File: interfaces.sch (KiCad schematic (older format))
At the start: 63 parts, among them IC3 TPD8S009DSMR, J4 WE_629105150521, J6 685119134923, J7 1140084168, Q2 BSS138AKA, Q3 BSS138AKA, Q4 BSS138AKA, Q5 BSS138AKA, Q6 BSS138AKA, U12 FT2232HQ

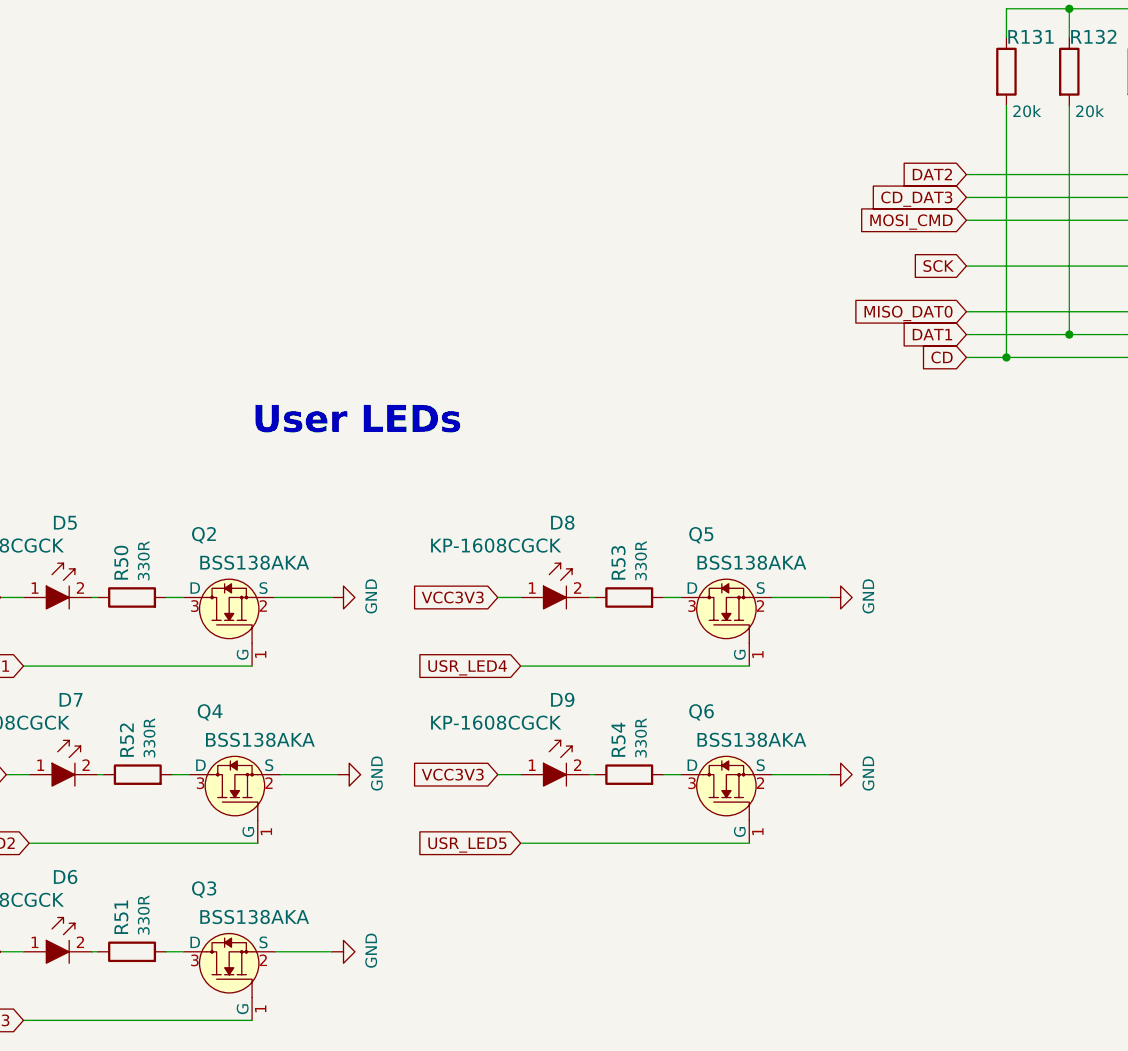
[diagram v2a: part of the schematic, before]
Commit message: Route SD card
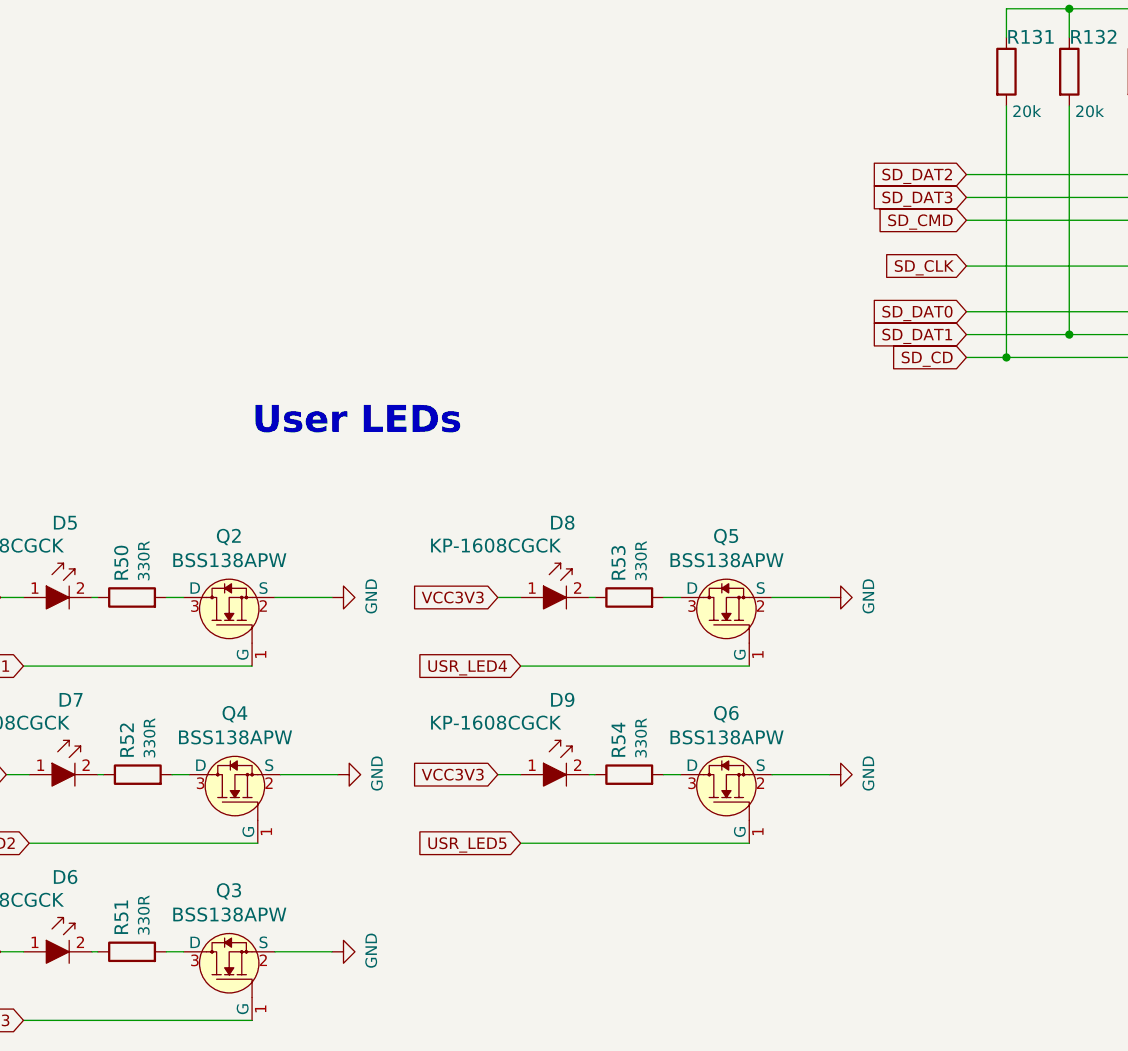
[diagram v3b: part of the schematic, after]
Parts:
- removed Q2, Q3, Q4, Q5, Q6: BSS138AKA, lpddr4-test-board-footprints:SOT-23-3, symbol lpddr4-test-board:BSS138AKA
- added Q2, Q3, Q4, Q5, Q6: BSS138APW, antmicro-footprints:SC70-3, symbol antmicroTransistorsFETsMOSFETsSingle:BSS138APW
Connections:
- net GND: now also Q2.2 (S), Q3.2 (S), Q4.2 (S), Q5.2 (S), Q6.2 (S)
- net USR_LED1: now also Q2.1 (G)
- net USR_LED2: now also Q4.1 (G)
- net USR_LED3: now also Q3.1 (G)
- net USR_LED4: now also Q5.1 (G)
- net USR_LED5: now also Q6.1 (G)
- net at R50.2: now also Q2.3 (D)
- net at R52.2: now also Q4.3 (D)
- net at R53.2: now also Q5.3 (D)
- net at R54.2: now also Q6.3 (D)
- net at R51.2: now also Q3.3 (D)
- net CD renamed SD_CD
- net CD_DAT3 renamed SD_DAT3
- net DAT1 renamed SD_DAT1
- net DAT2 renamed SD_DAT2
- net MISO_DAT0 renamed SD_DAT0
- net MOSI_CMD renamed SD_CMD
- net SCK renamed SD_CLK
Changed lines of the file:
@@
 Text GLabel 13300 6150 1    50   Input ~ 0
 VCC3V3
-Text GLabel 11125 6975 0    50   Input ~ 0
-DAT2
-Text GLabel 11125 7075 0    50   Input ~ 0
-CD_DAT3
-Text GLabel 11125 7175 0    50   Input ~ 0
-MOSI_CMD
-Text GLabel 11125 7375 0    50   Input ~ 0
-SCK
-Text GLabel 11125 7575 0    50   Input ~ 0
-MISO_DAT0
-Text GLabel 11125 7675 0    50   Input ~ 0
-DAT1
-Text GLabel 11125 7775 0    50   Input ~ 0
-CD
 Text Notes 3775 1450 0    118  ~ 24
 Debug UART
@@
 Wire Wire Line
 	7800 5900 7800 6000
-$Comp
-L lpddr4-test-board:BSS138AKA Q2
-U 1 1 5FF5BCFF
-P 7900 8825
-F 0 "Q2" V 8175 8875 60  0000 L CNN
-F 1 "BSS138AKA" V 8050 8475 60  0000 L CNN
-F 2 "lpddr4-test-board-footprints:SOT-23-3" H 8100 9025 60  0001 L CNN
-F 3 "https://www.onsemi.com/pub/Collateral/BSS138-D.PDF" H 8100 9125 60  0001 L CNN
-F 4 "BSS138AKAR" H 8100 9325 60  0001 L CNN "MPN"
-F 5 "ON Semiconductor" H 8100 9925 60  0001 L CNN "Manufacturer"
-	1    7900 8825
-	0    -1   -1   0
-$EndComp
 $Comp
 L lpddr4-test-board:GND #PWR0167
@@
 	8000 9125 7000 9125
 $Comp
-L lpddr4-test-board:BSS138AKA Q4
-U 1 1 6002240B
-P 7925 9600
-F 0 "Q4" V 8200 9650 60  0000 L CNN
-F 1 "BSS138AKA" V 8075 9250 60  0000 L CNN
-F 2 "lpddr4-test-board-footprints:SOT-23-3" H 8125 9800 60  0001 L CNN
-F 3 "https://www.onsemi.com/pub/Collateral/BSS138-D.PDF" H 8125 9900 60  0001 L CNN
-F 4 "BSS138AKAR" H 8125 10100 60  0001 L CNN "MPN"
-F 5 "ON Semiconductor" H 8125 10700 60  0001 L CNN "Manufacturer"
-	1    7925 9600
-	0    -1   -1   0
-$EndComp
-$Comp
 L lpddr4-test-board:GND #PWR0168
 U 1 1 60022411
@@
 	8025 9900 7025 9900
 $Comp
-L lpddr4-test-board:BSS138AKA Q5
-U 1 1 600304B1
-P 10075 8825
-F 0 "Q5" V 10350 8875 60  0000 L CNN
-F 1 "BSS138AKA" V 10225 8475 60  0000 L CNN
-F 2 "lpddr4-test-board-footprints:SOT-23-3" H 10275 9025 60  0001 L CNN
-F 3 "https://www.onsemi.com/pub/Collateral/BSS138-D.PDF" H 10275 9125 60  0001 L CNN
-F 4 "BSS138AKAR" H 10275 9325 60  0001 L CNN "MPN"
-F 5 "ON Semiconductor" H 10275 9925 60  0001 L CNN "Manufacturer"
-	1    10075 8825
-	0    -1   -1   0
-$EndComp
-$Comp
 L lpddr4-test-board:GND #PWR0169
 U 1 1 600304B7
@@
 	10175 9125 9175 9125
 $Comp
-L lpddr4-test-board:BSS138AKA Q6
-U 1 1 6003D8CD
-P 10075 9600
-F 0 "Q6" V 10350 9650 60  0000 L CNN
-F 1 "BSS138AKA" V 10225 9250 60  0000 L CNN
-F 2 "lpddr4-test-board-footprints:SOT-23-3" H 10275 9800 60  0001 L CNN
-F 3 "https://www.onsemi.com/pub/Collateral/BSS138-D.PDF" H 10275 9900 60  0001 L CNN
-F 4 "BSS138AKAR" H 10275 10100 60  0001 L CNN "MPN"
-F 5 "ON Semiconductor" H 10275 10700 60  0001 L CNN "Manufacturer"
-	1    10075 9600
-	0    -1   -1   0
-$EndComp
-$Comp
 L lpddr4-test-board:GND #PWR0170
 U 1 1 6003D8D3
@@
 Wire Wire Line
 	10175 9900 9175 9900
-$Comp
-L lpddr4-test-board:BSS138AKA Q3
-U 1 1 60050B08
-P 7900 10375
-F 0 "Q3" V 8175 10425 60  0000 L CNN
-F 1 "BSS138AKA" V 8050 10025 60  0000 L CNN
-F 2 "lpddr4-test-board-footprints:SOT-23-3" H 8100 10575 60  0001 L CNN
-F 3 "https://www.onsemi.com/pub/Collateral/BSS138-D.PDF" H 8100 10675 60  0001 L CNN
-F 4 "BSS138AKAR" H 8100 10875 60  0001 L CNN "MPN"
-F 5 "ON Semiconductor" H 8100 11475 60  0001 L CNN "Manufacturer"
-	1    7900 10375
-	0    -1   -1   0
-$EndComp
 $Comp
 L lpddr4-test-board:GND #PWR0171
@@
 Text Notes 8000 8125 0    118  ~ 24
 User LEDs
+$Comp
+L antmicroTransistorsFETsMOSFETsSingle:BSS138APW Q2
+U 1 1 6090FD8D
+P 7900 8825
+F 0 "Q2" V 8167 8825 60  0000 C CNN
+F 1 "BSS138APW" V 8061 8825 60  0000 C CNN
+F 2 "antmicro-footprints:SC70-3" H 8100 9025 60  0001 L CNN
+F 3 "" H 8100 9125 60  0001 L CNN
+F 4 "BSS138PW" H 8100 9325 60  0001 L CNN "MPN"
+F 5 "ON Semiconductor" H 8100 9925 60  0001 L CNN "Manufacturer"
+	1    7900 8825
+	0    -1   -1   0
+$EndComp
+$Comp
+L antmicroTransistorsFETsMOSFETsSingle:BSS138APW Q4
+U 1 1 6091F8AC
+P 7925 9600
+F 0 "Q4" V 8192 9600 60  0000 C CNN
+F 1 "BSS138APW" V 8086 9600 60  0000 C CNN
+F 2 "antmicro-footprints:SC70-3" H 8125 9800 60  0001 L CNN
+F 3 "" H 8125 9900 60  0001 L CNN
+F 4 "BSS138PW" H 8125 10100 60  0001 L CNN "MPN"
+F 5 "ON Semiconductor" H 8125 10700 60  0001 L CNN "Manufacturer"
+	1    7925 9600
+	0    -1   -1   0
+$EndComp
+$Comp
+L antmicroTransistorsFETsMOSFETsSingle:BSS138APW Q5
+U 1 1 6092108D
+P 10075 8825
+F 0 "Q5" V 10342 8825 60  0000 C CNN
+F 1 "BSS138APW" V 10236 8825 60  0000 C CNN
+F 2 "antmicro-footprints:SC70-3" H 10275 9025 60  0001 L CNN
+F 3 "" H 10275 9125 60  0001 L CNN
+F 4 "BSS138PW" H 10275 9325 60  0001 L CNN "MPN"
+F 5 "ON Semiconductor" H 10275 9925 60  0001 L CNN "Manufacturer"
+	1    10075 8825
+	0    -1   -1   0
+$EndComp
+$Comp
+L antmicroTransistorsFETsMOSFETsSingle:BSS138APW Q6
+U 1 1 60922535
+P 10075 9600
+F 0 "Q6" V 10342 9600 60  0000 C CNN
+F 1 "BSS138APW" V 10236 9600 60  0000 C CNN
+F 2 "antmicro-footprints:SC70-3" H 10275 9800 60  0001 L CNN
+F 3 "" H 10275 9900 60  0001 L CNN
+F 4 "BSS138PW" H 10275 10100 60  0001 L CNN "MPN"
+F 5 "ON Semiconductor" H 10275 10700 60  0001 L CNN "Manufacturer"
+	1    10075 9600
+	0    -1   -1   0
+$EndComp
+$Comp
+L antmicroTransistorsFETsMOSFETsSingle:BSS138APW Q3
+U 1 1 60923B88
+P 7900 10375
+F 0 "Q3" V 8167 10375 60  0000 C CNN
+F 1 "BSS138APW" V 8061 10375 60  0000 C CNN
+F 2 "antmicro-footprints:SC70-3" H 8100 10575 60  0001 L CNN
+F 3 "" H 8100 10675 60  0001 L CNN
+F 4 "BSS138PW" H 8100 10875 60  0001 L CNN "MPN"
+F 5 "ON Semiconductor" H 8100 11475 60  0001 L CNN "Manufacturer"
+	1    7900 10375
+	0    -1   -1   0
+$EndComp
+Text GLabel 11125 7775 0    50   Input ~ 0
+SD_CD
+Text GLabel 11125 6975 0    50   Input ~ 0
+SD_DAT2
+Text GLabel 11125 7675 0    50   Input ~ 0
+SD_DAT1
+Text GLabel 11125 7375 0    50   Input ~ 0
+SD_CLK
+Text GLabel 11125 7575 0    50   Input ~ 0
+SD_DAT0
+Text GLabel 11125 7175 0    50   Input ~ 0
+SD_CMD
+Text GLabel 11125 7075 0    50   Input ~ 0
+SD_DAT3
 $EndSCHEMATC

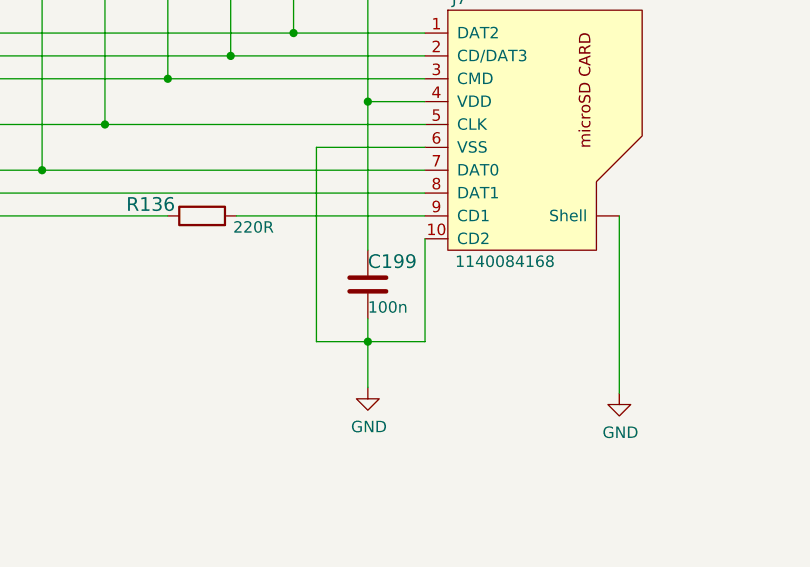
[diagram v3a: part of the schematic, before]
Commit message: Routed configuration block
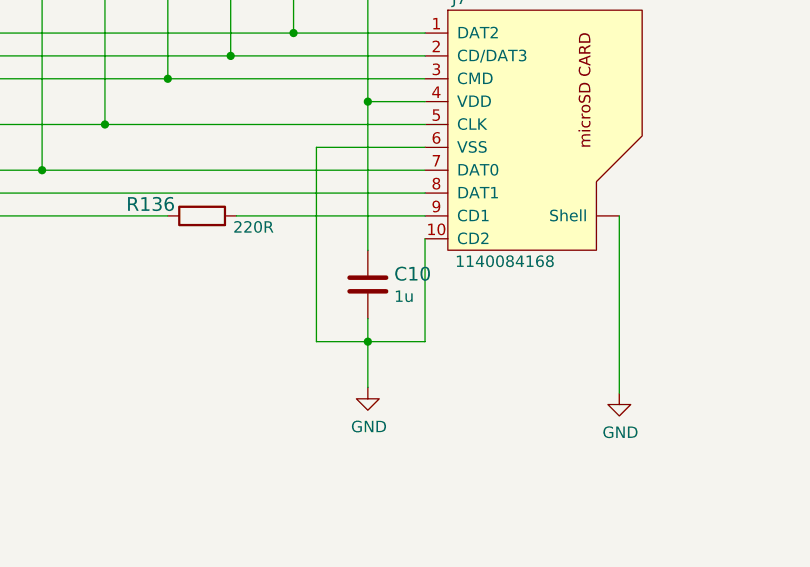
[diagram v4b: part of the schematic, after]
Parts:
- removed C199: C_100n_0402_6V3, lpddr4-test-board-footprints:0402-cap, symbol lpddr4-test-board:C_100n_0402_6V3
- added C10: C_1u_0603, antmicro-footprints:0603-cap, symbol antmicroCapacitors0603:C_1u_0603
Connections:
- net GND: now also C10.2
- net VCC3V3: now also C10.1
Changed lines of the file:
@@
 Wire Wire Line
 	11300 7775 11300 6675
-$Comp
-L lpddr4-test-board:C_100n_0402_6V3 C199
-U 1 1 60363EA1
-P 13300 8075
-F 0 "C199" H 13300 8175 60  0000 L CNN
-F 1 "C_100n_0402_6V3" H 13300 7925 60  0001 C CNN
-F 2 "lpddr4-test-board-footprints:0402-cap" H 13500 8275 60  0001 L CNN
-F 3 "" H 13300 8075 50  0001 C CNN
-F 4 "Walsin" H 13500 8475 60  0001 L CNN "Manufacturer"
-F 5 "0402X104K6R3CT" H 13500 8375 60  0001 L CNN "MPN"
-F 6 "100n" H 13300 7975 50  0000 L CNN "Val"
-	1    13300 8075
-	1    0    0    -1
-$EndComp
 Wire Wire Line
 	13300 7925 13300 7275
@@
 Text GLabel 11125 7075 0    50   Input ~ 0
 SD_DAT3
+$Comp
+L antmicroCapacitors0603:C_1u_0603 C10
+U 1 1 617CD12F
+P 13300 8075
+F 0 "C10" H 13415 8120 60  0000 L CNN
+F 1 "C_1u_0603" H 13300 7925 60  0001 C CNN
+F 2 "antmicro-footprints:0603-cap" H 13500 8275 60  0001 L CNN
+F 3 "" H 13300 8075 50  0001 C CNN
+F 4 "WALSIN" H 13500 8475 60  0001 L CNN "Manufacturer"
+F 5 "0603YD105KAT2A" H 13500 8375 60  0001 L CNN "MPN"
+F 6 "1u" H 13415 8022 50  0000 L CNN "Val"
+	1    13300 8075
+	1    0    0    -1
+$EndComp
 $EndSCHEMATC

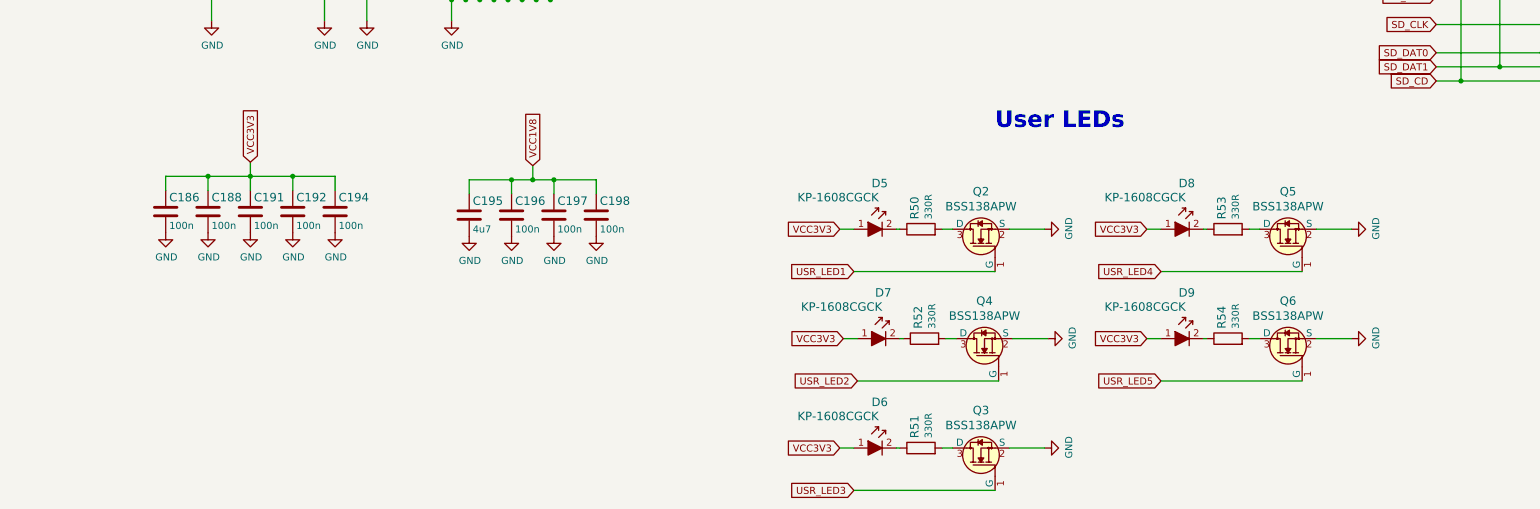
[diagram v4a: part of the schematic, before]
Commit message: Add User buttons to schematic
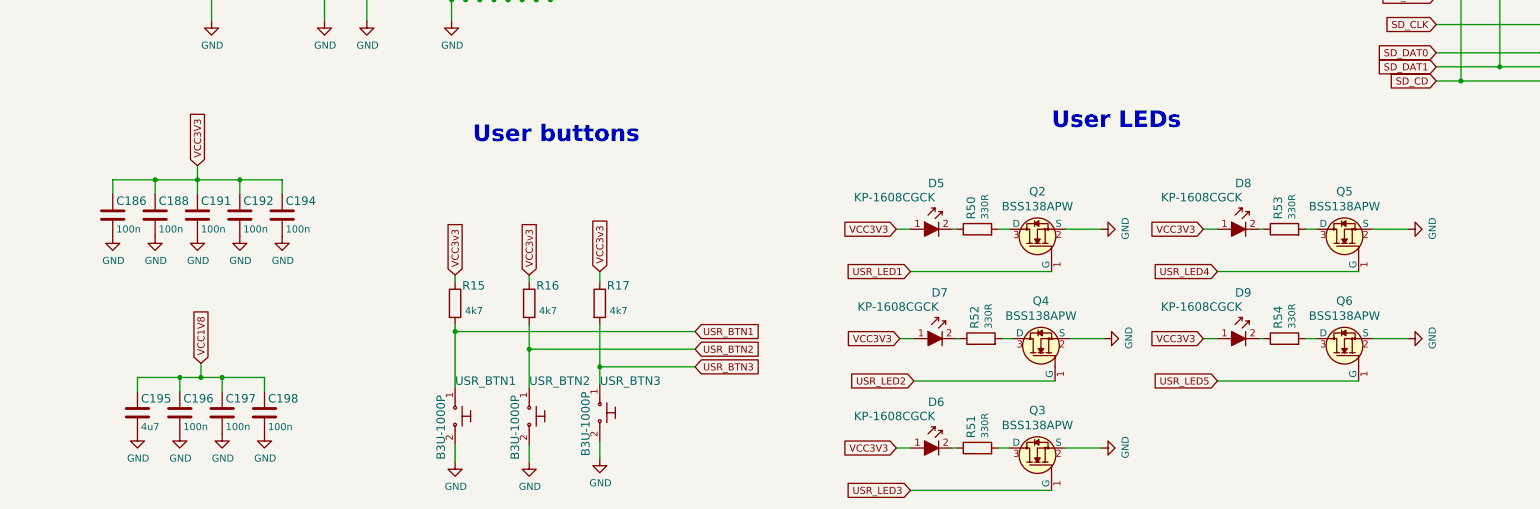
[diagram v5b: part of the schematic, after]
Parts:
- added R15, R16, R17: R_4k7_0402, lpddr4-test-board-footprints:0402-res, symbol lpddr4-test-board:R_4k7_0402
- added USR_BTN1, USR_BTN2, USR_BTN3: B3U-1000P, lpddr4-test-board-footprints:Switch_Tactile_SMD_B3U-1000P, symbol lpddr4-test-board:B3U-1000P
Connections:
- net GND: now also USR_BTN1.2, USR_BTN2.2, USR_BTN3.2
- new net USR_BTN1: R15.2, USR_BTN1.1
- new net USR_BTN2: R16.2, USR_BTN2.1
- new net USR_BTN3: R17.2, USR_BTN3.1
- new net VCC3v3: R15.1, R16.1, R17.1
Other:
- note added: "User buttons"
- moved on the sheet: C186, C188, C191, C192, C194, C195, C196, C197, C198, D5, D6, D7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
